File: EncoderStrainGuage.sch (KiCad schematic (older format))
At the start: 81 parts, among them IC1 LM60CIM3_NOPB, J1 Conn_01x05, J2 MM8130-2600RA2, J3 MM8130-2600RA2, J4 Rotary Encoder, J5 Conn_01x02_Male, J6 Conn_01x02_Male, J7 47219-2001, U1 PIC16LF88-I_SO, U2 OPAMP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

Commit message: "Fixed all routing"
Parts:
- removed C21, C22: 100n, Capacitor_SMD:C_0603_1608Metric, symbol EncoderStrainGuage-rescue:C-Device
- removed J4: Rotary Encoder, Connector_PinHeader_1.00mm:PinHeader_1x02_P1.00mm_Vertical, symbol EncoderStrainGuage-rescue:Conn_01x03_Male-Connector
- removed J5, J6: Conn_01x02_Male, Connector_PinHeader_1.00mm:PinHeader_1x02_P1.00mm_Vertical, symbol EncoderStrainGuage-rescue:Conn_01x02_Male-Connector
- removed U5: INA333AIDGKR, DFFP-master:INA333AIDGKR, symbol EncoderStrainGuage-rescue:INA333AIDGKR-amplifier_INA333AIDGKR
- removed VR1, VR2: StrainG 350 ohm, Connector_PinHeader_1.00mm:PinHeader_1x02_P1.00mm_Vertical, symbol EncoderStrainGuage-rescue:StrainGuage-EncoderBoard
- added J4: Conn_01x12, DFFP-master:1-1734595-2, symbol Connector_Generic:Conn_01x12
- added R18: 200k, Resistor_SMD:R_0603_1608Metric, symbol EncoderStrainGuage-rescue:R_US-Device
- added U5: MCP6N11T, DFFP-master:MCP6N11T-010E, symbol DFFPSymbols:MCP6N11T
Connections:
- net labels added: SSTB, Str1_Gnd, Str1_Str+, Str2_3v3, Str2_Str+
- wire segments 170 -> 182
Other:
- moved on the sheet: C14, C15, C4, J1, R5, R6, Y2

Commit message: Fixed RF stuff
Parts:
- removed FL1: LFB182G45BG2D280, LFB182G45BG2D280:LFB182G45BG5D920_1, symbol EncoderStrainGuage-rescue:LFB182G45BG2D280-LFB182G45BG2D280
- removed NP2: ?, Capacitor_SMD:C_0603_1608Metric, symbol EncoderStrainGuage-rescue:C-Device
- removed R2: 10k, Resistor_SMD:R_0603_1608Metric, symbol EncoderStrainGuage-rescue:R-Device
- removed R5, R6: 100, Resistor_SMD:R_0603_1608Metric, symbol EncoderStrainGuage-rescue:R-Device
- removed U1: PIC16LF88-I_SO, PIC16LF88-I_SO:SOIC127P1030X265-18N, symbol EncoderStrainGuage-rescue:PIC16LF88-I_SO-2019-12-16_16-51-55
- added C21: 18pF, Capacitor_SMD:C_0603_1608Metric, symbol EncoderStrainGuage-rescue:C-Device
- added C22, C33: 1pF, Capacitor_SMD:C_0603_1608Metric, symbol EncoderStrainGuage-rescue:C-Device
- added C35: .1u, Capacitor_SMD:C_0603_1608Metric, symbol EncoderStrainGuage-rescue:C-Device
- added IC2: PIC16LF1826-I_SO, Package_SO:SOIC-18W_7.5x11.6mm_P1.27mm, symbol DFFPSymbols:PIC16LF1826-I_SO
- added L7: 2nH, Inductor_SMD:L_0603_1608Metric_Pad1.05x0.95mm_HandSolder, symbol EncoderStrainGuage-rescue:L-Device
- added L8: 2nH, Inductor_SMD:L_0603_1608Metric, symbol EncoderStrainGuage-rescue:L-Device
- added L9: 1nH, Inductor_SMD:L_0603_1608Metric_Pad1.05x0.95mm_HandSolder, symbol EncoderStrainGuage-rescue:L-Device
- added R2, R6: 10k, Resistor_SMD:R_0603_1608Metric, symbol EncoderStrainGuage-rescue:R_US-Device
- added R5: 1k, Resistor_SMD:R_0603_1608Metric, symbol EncoderStrainGuage-rescue:R_US-Device
- C34: renamed from NP4; value ? -> 1pF
- C4: value 100n -> 18pF
- J1: footprint Connector_PinHeader_2.54mm:PinHeader_1x05_P2.54mm_Vertical -> Connector_PinSocket_2.54mm:PinSocket_1x05_P2.54mm_Vertical
- J4: symbol Connector_Generic:Conn_01x12 -> EncoderStrainGuage-rescue:Conn_01x12-Connector_Generic
- L10: renamed from NP3; value ? -> 3nH
- L4, L5, L6: symbol Device:L -> EncoderStrainGuage-rescue:L-Device
- RV1, RV2, RV3: symbol Device:R_POT_TRIM_US -> EncoderStrainGuage-rescue:R_POT_TRIM_US-Device
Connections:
- net Suspend is gone; now on net +3V3: U3.19 (*SUSPEND/*SRDY)
- net +3V3: now also J1.4 (Pin_4), IC2.14 (VDD), R2.2; no longer C4.1, J1.2 (Pin_2)
- net GND: now also J1.5 (Pin_5), C22.2, C35.2, IC2.5 (VSS), L7.1, R6.2; no longer C4.2, J1.3 (Pin_3)
- net MCLR: now also IC2.4 (RA5/~MCLR~/VPP), R5.1
- net MISO: now also IC2.15 (RA6)
- net MOSI: now also IC2.7 (RB1)
- net PSout: now also IC2.3 (RA4); no longer J4.5 (Pin_5), R3.2, U2.1 (+)
- net PotOut: now also IC2.1 (RA2)
- net RFneg: now also C21.1
- net RFpos: now also C4.1
- net RTS: now also IC2.6 (RB0)
- net Reset: now also IC2.17 (RA0)
- net SSTB: now also IC2.18 (RA1)
- net Sleep: now also IC2.16 (RA7)
- net Str-: now also RV1.2, RV2.2; no longer RV1.3, RV2.1
- net Str1: now also IC2.9 (RB3)
- net TempOut: now also IC2.2 (RA3)
- net UARTrx: now also IC2.8 (RB2)
- net UARTtx: now also IC2.11 (RB5)
- net at L10.1: now also J3.IN; no longer C34.1
- net at L10.2: now also C34.1, L9.1; no longer J3.IN
- net SD_CS: no longer names the net of J7.2 (CD/DAT3)
- net SD_CS: now also R6.1
- new net: C33.1, C4.2, L7.2
- new net: C21.2, C22.1, L8.1
- new net: C33.2, L8.2, L9.2
- new net: C35.1, R2.1, R5.2
- new net ICSPCLK: IC2.12 (RB6), J1.2 (Pin_2)
- new net ICSPDAT: IC2.13 (RB7), J1.3 (Pin_3)
- new net PSin: J4.5 (Pin_5), R3.2, U2.1 (+)
- new net SCLK: IC2.10 (RB4)
- no-connect marks 2 -> 4
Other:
- moved on the sheet: C1, C34, L10

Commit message: Fixed trimmer
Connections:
- net GND: now also RV3.3; no longer RV3.1
- net at R18.2, U5.1 (VFG): now also RV3.2; no longer RV3.3
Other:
- moved on the sheet: RV3
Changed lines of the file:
@@
 Wire Wire Line
 	21400 5200 20750 5200
-Wire Wire Line
-	20750 5200 20750 5250
-Wire Wire Line
-	20750 5550 20750 5600
 $Comp
 L EncoderStrainGuage-rescue:GND-power #PWR0179
@@
 L EncoderStrainGuage-rescue:R_POT_TRIM_US-Device RV3
 U 1 1 5E538453
-P 20750 5400
-F 0 "RV3" V 20545 5400 50  0000 C CNN
-F 1 "10k TRIM" V 20636 5400 50  0000 C CNN
-F 2 "DFFP-master:TC33X-2_1" H 20750 5400 50  0001 C CNN
-F 3 "~" H 20750 5400 50  0001 C CNN
-	1    20750 5400
-	-1   0    0    1
+P 20600 5600
+F 0 "RV3" V 20395 5600 50  0000 C CNN
+F 1 "10k TRIM" V 20486 5600 50  0000 C CNN
+F 2 "DFFP-master:TC33X-2_1" H 20600 5600 50  0001 C CNN
+F 3 "~" H 20600 5600 50  0001 C CNN
+	1    20600 5600
+	0    -1   -1   0
 $EndComp
 Wire Wire Line
@@
 	-1   0    0    1
 $EndComp
+Wire Wire Line
+	20600 5450 20600 5200
+Wire Wire Line
+	20600 5200 20750 5200
 $EndSCHEMATC

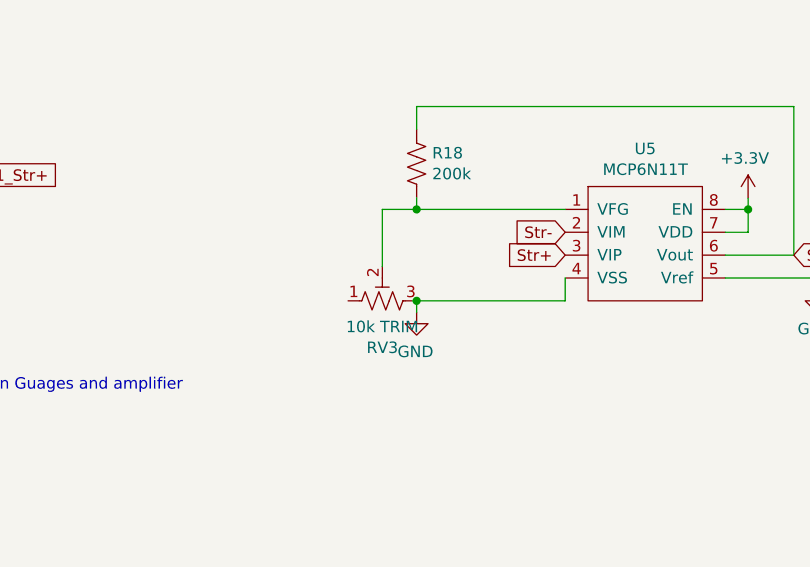
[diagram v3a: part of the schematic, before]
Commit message: Improved RF routing
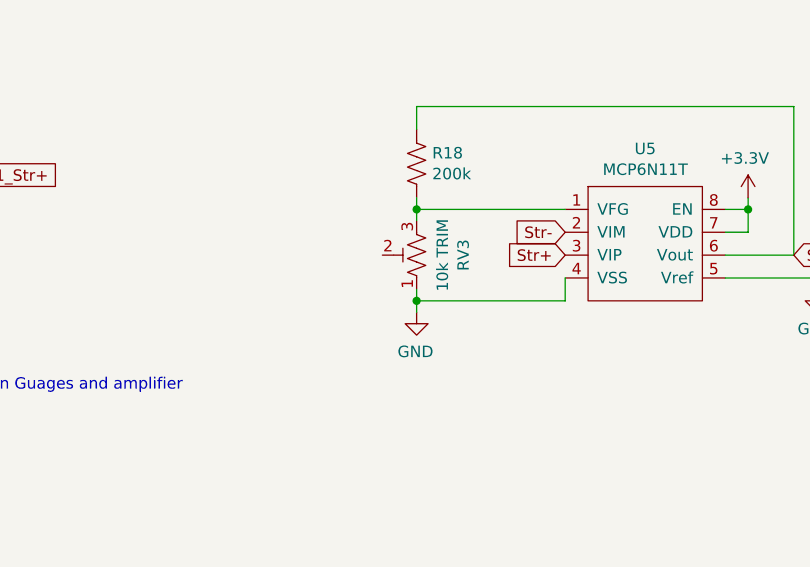
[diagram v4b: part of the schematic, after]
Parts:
- C21, C22, C33, C34, C4: footprint Capacitor_SMD:C_0603_1608Metric -> Capacitor_SMD:C_0402_1005Metric
- L10, L7, L9: footprint Inductor_SMD:L_0603_1608Metric_Pad1.05x0.95mm_HandSolder -> Inductor_SMD:L_0402_1005Metric
- L8: footprint Inductor_SMD:L_0603_1608Metric -> Inductor_SMD:L_0402_1005Metric
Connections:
- net GND: now also RV3.1; no longer RV3.3
- net at R18.2, U5.1 (VFG): now also RV3.3; no longer RV3.2
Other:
- moved on the sheet: RV3
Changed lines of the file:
@@
 F 0 "C34" H 12165 13813 50  0000 L CNN
 F 1 "1pF" H 12056 13734 35  0000 L CNN
-F 2 "Capacitor_SMD:C_0603_1608Metric" H 12088 13750 50  0001 C CNN
+F 2 "Capacitor_SMD:C_0402_1005Metric" H 12088 13750 50  0001 C CNN
 F 3 "~" H 12050 13900 50  0001 C CNN
 	1    12050 13900
@@
 F 0 "L10" V 11619 14050 50  0000 C CNN
 F 1 "3nH" V 11710 14050 35  0000 C CNN
-F 2 "Inductor_SMD:L_0603_1608Metric_Pad1.05x0.95mm_HandSolder" H 11800 14050 50  0001 C CNN
+F 2 "Inductor_SMD:L_0402_1005Metric" H 11800 14050 50  0001 C CNN
 F 3 "~" H 11800 14050 50  0001 C CNN
 	1    11800 14050
@@
 Wire Wire Line
 	21400 5200 20750 5200
+Wire Wire Line
+	20750 5200 20750 5250
+Wire Wire Line
+	20750 5550 20750 5600
 $Comp
 L EncoderStrainGuage-rescue:GND-power #PWR0179
@@
 L EncoderStrainGuage-rescue:R_POT_TRIM_US-Device RV3
 U 1 1 5E538453
-P 20600 5600
-F 0 "RV3" V 20395 5600 50  0000 C CNN
-F 1 "10k TRIM" V 20486 5600 50  0000 C CNN
-F 2 "DFFP-master:TC33X-2_1" H 20600 5600 50  0001 C CNN
-F 3 "~" H 20600 5600 50  0001 C CNN
-	1    20600 5600
-	0    -1   -1   0
+P 20750 5400
+F 0 "RV3" V 20545 5400 50  0000 C CNN
+F 1 "10k TRIM" V 20636 5400 50  0000 C CNN
+F 2 "DFFP-master:TC33X-2_1" H 20750 5400 50  0001 C CNN
+F 3 "~" H 20750 5400 50  0001 C CNN
+	1    20750 5400
+	-1   0    0    1
 $EndComp
 Wire Wire Line
@@
 F 0 "C21" H 11015 13413 50  0000 L CNN
 F 1 "18pF" H 10906 13334 35  0000 L CNN
-F 2 "Capacitor_SMD:C_0603_1608Metric" H 10938 13350 50  0001 C CNN
+F 2 "Capacitor_SMD:C_0402_1005Metric" H 10938 13350 50  0001 C CNN
 F 3 "~" H 10900 13500 50  0001 C CNN
 	1    10900 13500
@@
 F 0 "C22" H 11315 13563 50  0000 L CNN
 F 1 "1pF" H 11206 13484 35  0000 L CNN
-F 2 "Capacitor_SMD:C_0603_1608Metric" H 11238 13500 50  0001 C CNN
+F 2 "Capacitor_SMD:C_0402_1005Metric" H 11238 13500 50  0001 C CNN
 F 3 "~" H 11200 13650 50  0001 C CNN
 	1    11200 13650
@@
 F 0 "L8" V 11369 13500 50  0000 C CNN
 F 1 "2nH" V 11460 13500 35  0000 C CNN
-F 2 "Inductor_SMD:L_0603_1608Metric" H 11550 13500 50  0001 C CNN
+F 2 "Inductor_SMD:L_0402_1005Metric" H 11550 13500 50  0001 C CNN
 F 3 "~" H 11550 13500 50  0001 C CNN
 	1    11550 13500
@@
 F 0 "C33" H 11665 13063 50  0000 L CNN
 F 1 "1pF" H 11556 12984 35  0000 L CNN
-F 2 "Capacitor_SMD:C_0603_1608Metric" H 11588 13000 50  0001 C CNN
+F 2 "Capacitor_SMD:C_0402_1005Metric" H 11588 13000 50  0001 C CNN
 F 3 "~" H 11550 13150 50  0001 C CNN
 	1    11550 13150
@@
 F 0 "L7" V 11019 13000 50  0000 C CNN
 F 1 "2nH" V 11110 13000 35  0000 C CNN
-F 2 "Inductor_SMD:L_0603_1608Metric_Pad1.05x0.95mm_HandSolder" H 11200 13000 50  0001 C CNN
+F 2 "Inductor_SMD:L_0402_1005Metric" H 11200 13000 50  0001 C CNN
 F 3 "~" H 11200 13000 50  0001 C CNN
 	1    11200 13000
@@
 F 0 "C4" H 11015 13063 50  0000 L CNN
 F 1 "18pF" H 10906 12984 35  0000 L CNN
-F 2 "Capacitor_SMD:C_0603_1608Metric" H 10938 13000 50  0001 C CNN
+F 2 "Capacitor_SMD:C_0402_1005Metric" H 10938 13000 50  0001 C CNN
 F 3 "~" H 10900 13150 50  0001 C CNN
 	1    10900 13150
@@
 F 0 "L9" V 11619 13750 50  0000 C CNN
 F 1 "1nH" V 11710 13750 35  0000 C CNN
-F 2 "Inductor_SMD:L_0603_1608Metric_Pad1.05x0.95mm_HandSolder" H 11800 13750 50  0001 C CNN
+F 2 "Inductor_SMD:L_0402_1005Metric" H 11800 13750 50  0001 C CNN
 F 3 "~" H 11800 13750 50  0001 C CNN
 	1    11800 13750
@@
 	-1   0    0    1
 $EndComp
-Wire Wire Line
-	20600 5450 20600 5200
-Wire Wire Line
-	20600 5200 20750 5200
 $EndSCHEMATC
